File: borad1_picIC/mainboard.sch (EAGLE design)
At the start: 23 parts, among them IC2 7805TV, K1 G6RW

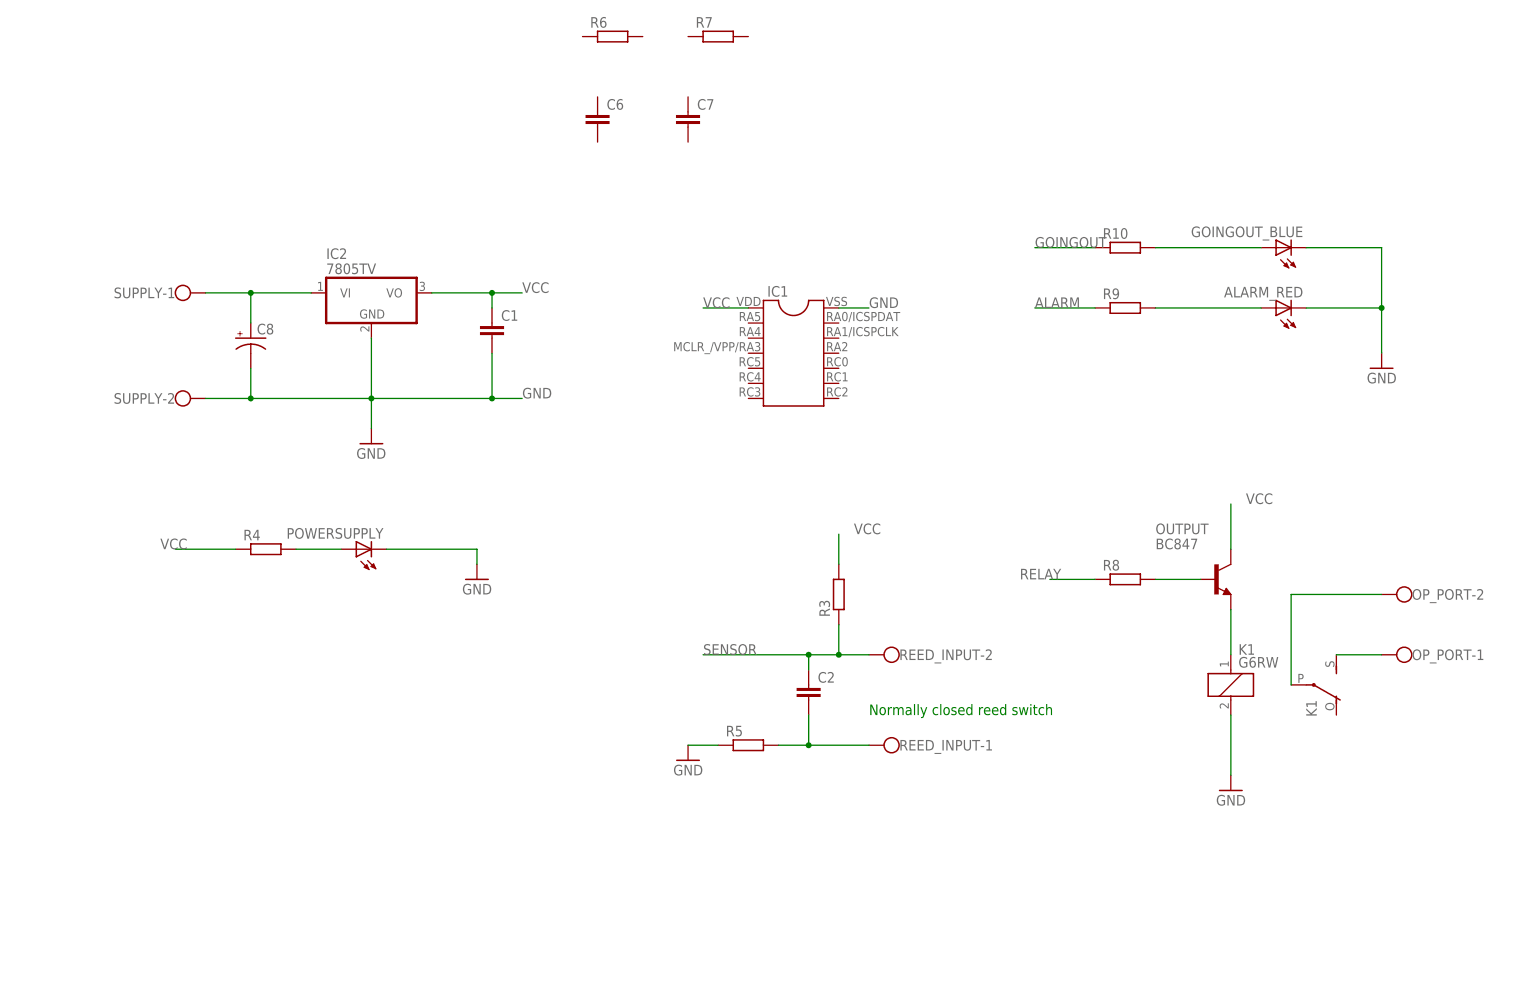
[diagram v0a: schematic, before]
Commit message: First board ready, just figuring out the placement and connectors.
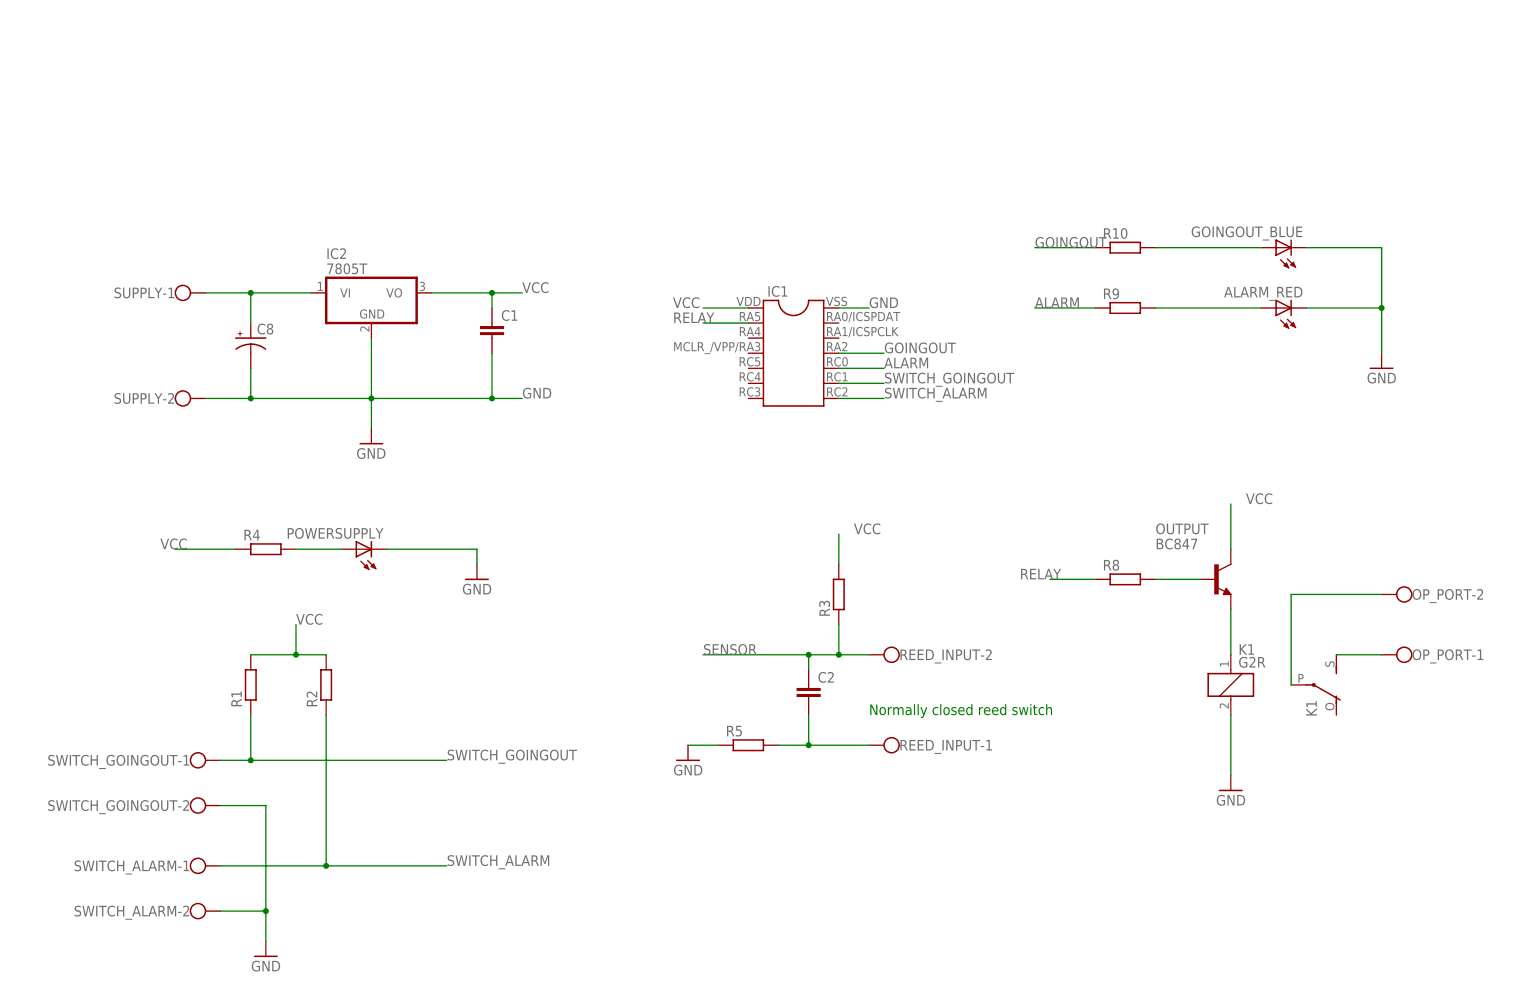
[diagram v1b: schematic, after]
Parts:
- removed C6, C7: (no value), eagle-ltspice:CC0603
- removed R6, R7: (no value), rcl:R-EU_R0603
- added R1, R2: (no value), rcl:R-EU_R0603
- added SWITCH_ALARM, SWITCH_GOINGOUT: (no value), con-wago-500:W237-102
- IC2: value 7805TV -> 7805T; device linear:7805TV -> linear:7805T
- K1: value G6RW -> G2R; device relay:G6RW -> relay:G2R
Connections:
- new net SWITCH_ALARM: IC1.8, R2.1, SWITCH_ALARM-1.KL
- new net SWITCH_GOINGOUT: IC1.9, R1.1, SWITCH_GOINGOUT-1.KL
- net ALARM: now also IC1.10
- net GND: now also SWITCH_ALARM-2.KL, SWITCH_GOINGOUT-2.KL
- net GOINGOUT: now also IC1.11
- net RELAY: now also IC1.2
- net VCC: now also R1.2, R2.2

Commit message: Converting everything thing to SMD, All the wires routed, components and connection modified as per suggestion from senior
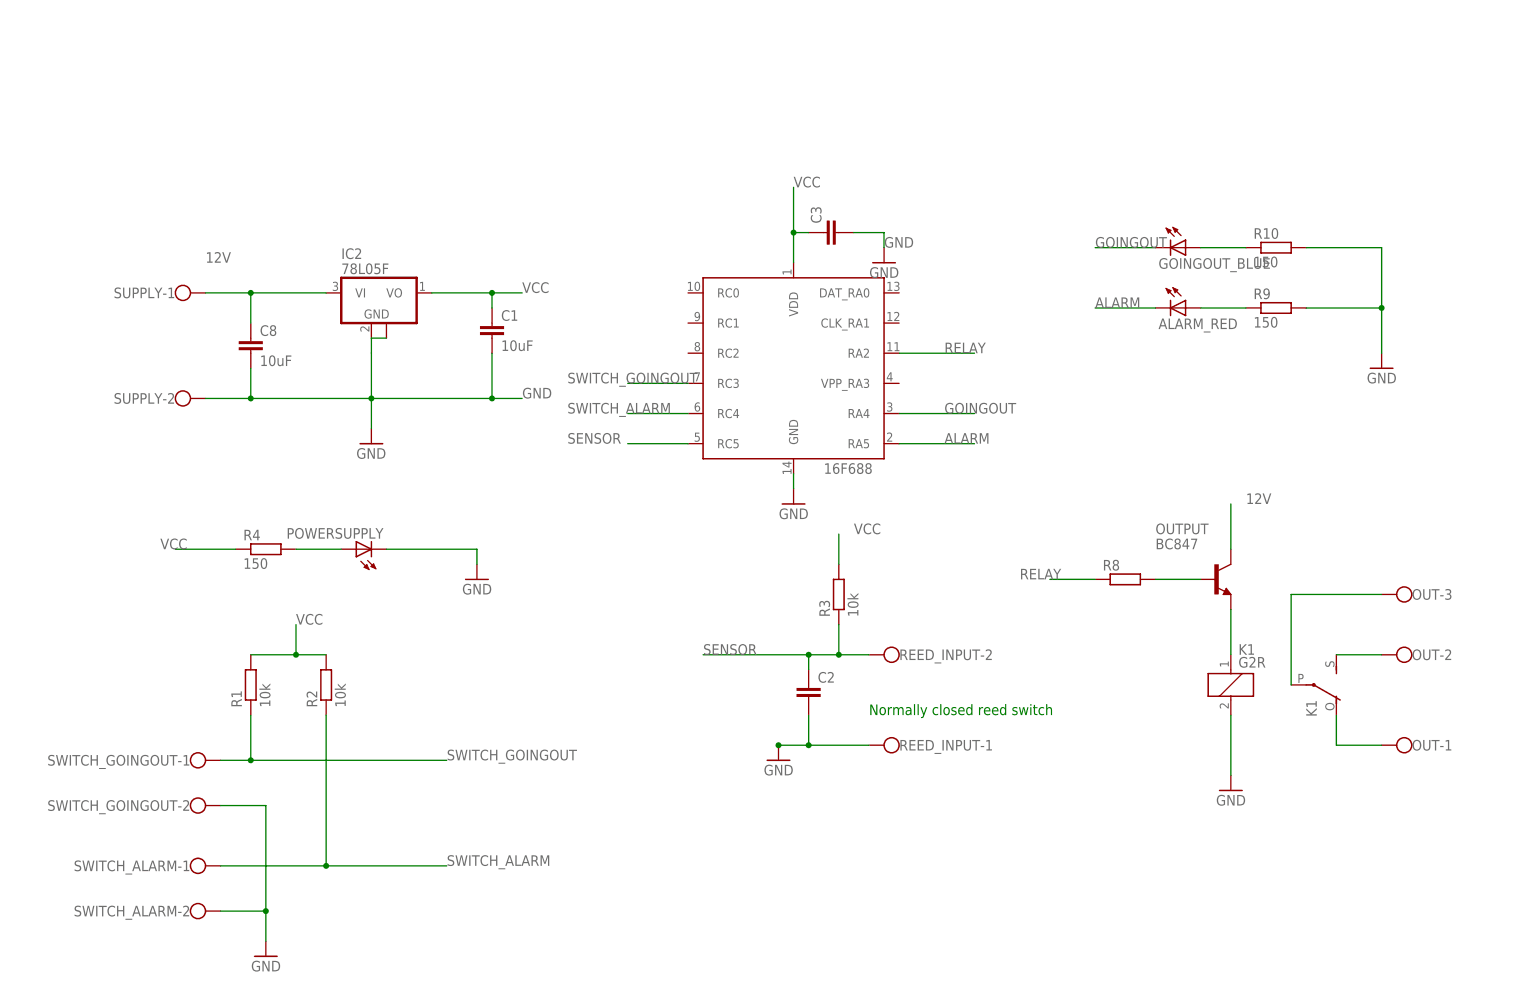
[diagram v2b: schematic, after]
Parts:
- removed IC1: (no value), pic16f1824_mack:DIL14
- removed OP_PORT: (no value), con-wago-500:W237-102
- removed R5: (no value), rcl:R-EU_R0603
- added C3: (no value), rcl:C-EUC0805
- added OUT: (no value), con-wago-500:W237-103
- added U$1: (no value), microchip-16f688:PIC16F688SOIC14
- C1: value (none) -> 10uF; device eagle-ltspice:CC0603 -> rcl:C-EUC0805
- C8: value (none) -> 10uF; device rcl:CPOL-USE2.5-5 -> rcl:C-EUC0805
- IC2: value 7805T -> 78L05F; device linear:7805T -> linear:78L05F
- R1, R2, R3: value (none) -> 10k
- R10, R4, R9: value (none) -> 150
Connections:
- removed net N$7: C2.2, R5.2, REED_INPUT-1.KL
- new net 12V: C8.1, IC2.VI, OUTPUT.C, SUPPLY-1.KL
- net ALARM: now also ALARM_RED.C, U$1.RA5; no longer IC1.10, R9.1
- net GND: now also C2.2, C3.2, C8.2, IC2.GND@1, R10.2, R9.2, REED_INPUT-1.KL, U$1.GND; no longer ALARM_RED.C, C8.-, GOINGOUT_BLUE.C, IC1.14, R5.1
- net GOINGOUT: now also GOINGOUT_BLUE.C, U$1.RA4; no longer IC1.11, R10.1
- net N$1: now also K12.O, OUT-1.KL; no longer C8.+, IC2.VI, SUPPLY-1.KL
- net N$2: now also R10.1; no longer R10.2
- net N$5: now also R9.1; no longer R9.2
- net N$8: now also OUT-3.KL; no longer OP_PORT-2.KL
- net N$9: now also OUT-2.KL; no longer OP_PORT-1.KL
- net RELAY: now also U$1.RA2; no longer IC1.2
- net SENSOR: now also U$1.RC5
- net SWITCH_ALARM: now also U$1.RC4; no longer IC1.8
- net SWITCH_GOINGOUT: now also U$1.RC3; no longer IC1.9
- net VCC: now also C3.1, U$1.VDD; no longer IC1.1, OUTPUT.C
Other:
- moved on the sheet: ALARM_RED, GOINGOUT_BLUE, R10, R9

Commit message: Changing Relay foot print to available relay and rerouted the whole PCB
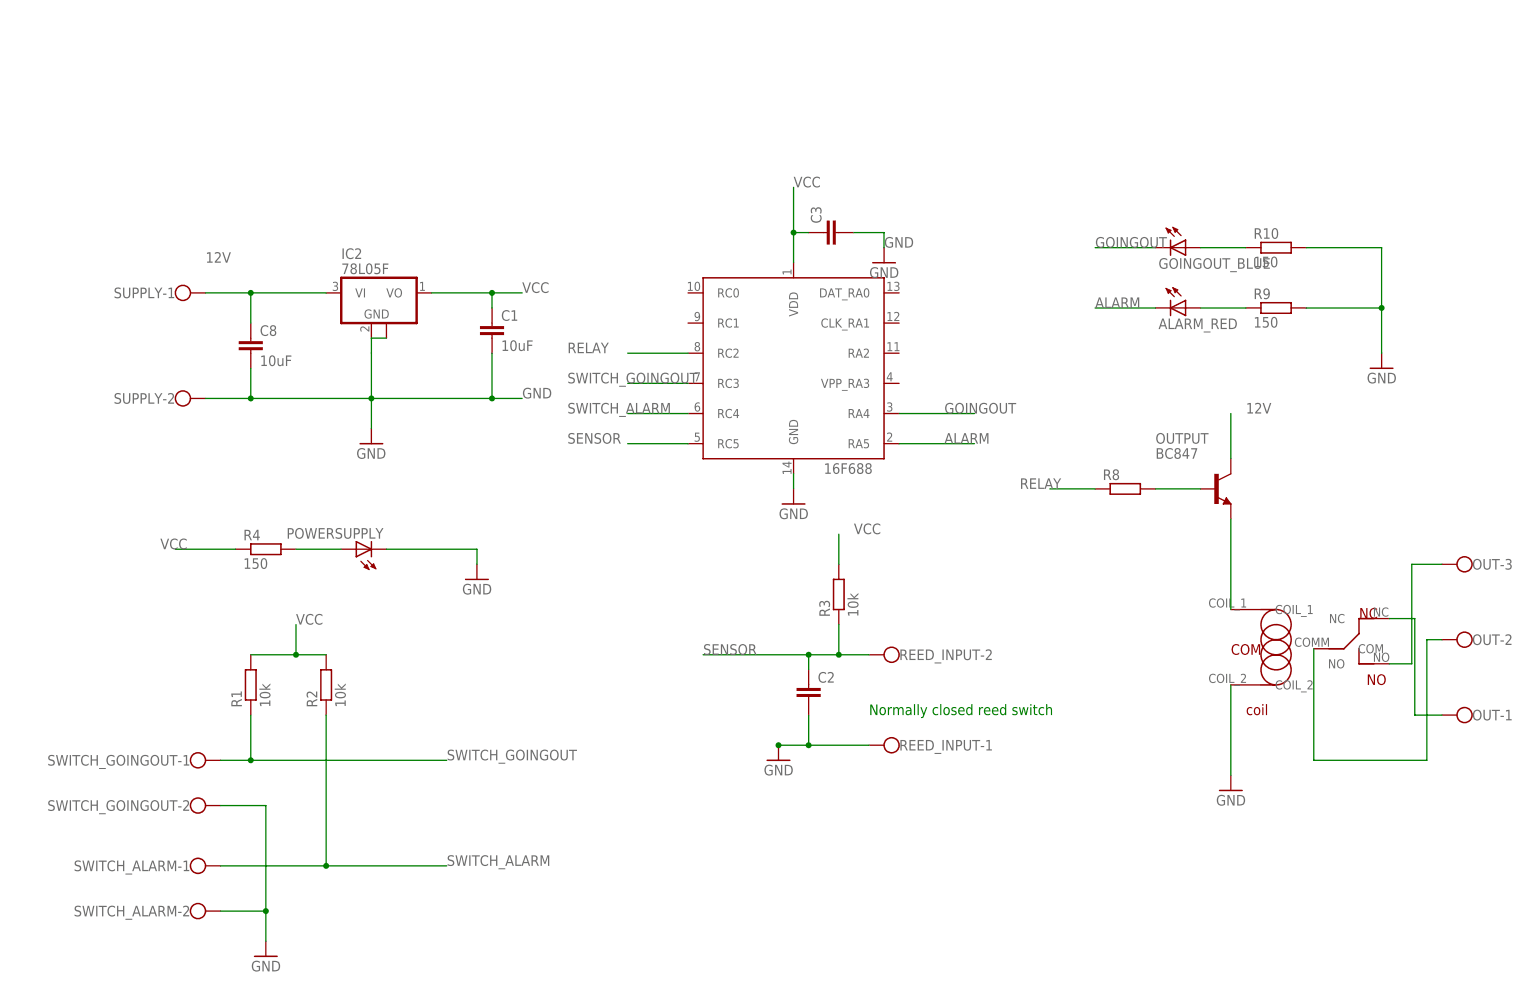
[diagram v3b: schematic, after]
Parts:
- removed K1: G2R, relay:G2R
- added U$2: (no value), JQC-3FC_relay:JQC-3FC_RELAY
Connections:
- net GND: now also U$2.COIL_2; no longer K11.2
- net N$1: now also OUTPUT.E, U$2.COIL_1; no longer K12.O, OUT-1.KL
- net N$6: now also OUT-1.KL, U$2.NC; no longer K11.1, OUTPUT.E
- net N$8: now also U$2.NO; no longer K12.P
- net N$9: now also U$2.COM; no longer K12.S
- net RELAY: now also U$1.RC2; no longer U$1.RA2
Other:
- moved on the sheet: OUT-1, OUT-2, OUT-3, OUTPUT, R8
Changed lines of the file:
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@@
 <?xml version="1.0" encoding="utf-8"?>
 <!DOCTYPE eagle SYSTEM "eagle.dtd">
-<eagle version="7.2.0">
+<eagle version="7.5.0">
 <drawing>
 <settings>
@@
 <part name="ALARM_RED" library="led" deviceset="LED" device="5MM"/>
 <part name="OUTPUT" library="transistor" deviceset="BC847" device=""/>
-<part name="K1" library="relay" deviceset="G2R" device=""/>
 <part name="REED_INPUT" library="con-wago-500" deviceset="W237-102" device=""/>
 <part name="SUPPLY" library="con-wago-500" deviceset="W237-102" device=""/>
@@
 <part name="GND7" library="supply1" deviceset="GND" device=""/>
 <part name="GND8" library="supply1" deviceset="GND" device=""/>
+<part name="U$2" library="JQC-3FC_relay" deviceset="JQC-3FC_RELAY" device=""/>
 </parts>
 <sheets>
@@
 <instance part="R3" gate="G$1" x="134.62" y="71.12" rot="R90"/>
 <instance part="R4" gate="G$1" x="38.1" y="78.74"/>
-<instance part="R8" gate="G$1" x="182.88" y="73.66"/>
+<instance part="R8" gate="G$1" x="182.88" y="88.9"/>
 <instance part="R9" gate="G$1" x="208.28" y="119.38"/>
 <instance part="R10" gate="G$1" x="208.28" y="129.54"/>
@@
 <instance part="GOINGOUT_BLUE" gate="G$1" x="193.04" y="129.54" rot="R270"/>
 <instance part="ALARM_RED" gate="G$1" x="193.04" y="119.38" rot="R270"/>
-<instance part="OUTPUT" gate="G$1" x="198.12" y="73.66"/>
-<instance part="K1" gate="1" x="200.66" y="55.88"/>
-<instance part="K1" gate="2" x="213.36" y="55.88" rot="R270"/>
+<instance part="OUTPUT" gate="G$1" x="198.12" y="88.9"/>
 <instance part="REED_INPUT" gate="-1" x="144.78" y="45.72" rot="R180"/>
 <instance part="REED_INPUT" gate="-2" x="144.78" y="60.96" rot="R180"/>
@@
 <instance part="R2" gate="G$1" x="48.26" y="55.88" rot="R90"/>
 <instance part="GND6" gate="1" x="38.1" y="10.16" rot="MR0"/>
-<instance part="OUT" gate="-1" x="231.14" y="45.72" rot="R180"/>
-<instance part="OUT" gate="-2" x="231.14" y="60.96" rot="R180"/>
-<instance part="OUT" gate="-3" x="231.14" y="71.12" rot="R180"/>
+<instance part="OUT" gate="-1" x="241.3" y="50.8" rot="R180"/>
+<instance part="OUT" gate="-2" x="241.3" y="63.5" rot="R180"/>
+<instance part="OUT" gate="-3" x="241.3" y="76.2" rot="R180"/>
 <instance part="C3" gate="G$1" x="132.08" y="132.08" rot="R90"/>
 <instance part="U$1" gate="NAME" x="127" y="111.76"/>
 <instance part="GND7" gate="1" x="142.24" y="127" rot="MR0"/>
 <instance part="GND8" gate="1" x="127" y="86.36" rot="MR0"/>
+<instance part="U$2" gate="G$1" x="246.38" y="50.8"/>
 </instances>
 <busses>
@@
 <segment>
 <pinref part="OUTPUT" gate="G$1" pin="C"/>
-<wire x1="200.66" y1="78.74" x2="200.66" y2="86.36" width="0.1524" layer="91"/>
-<label x="203.2" y="86.36" size="1.778" layer="95"/>
+<wire x1="200.66" y1="93.98" x2="200.66" y2="101.6" width="0.1524" layer="91"/>
+<label x="203.2" y="101.6" size="1.778" layer="95"/>
 </segment>
 </net>
@@
 </segment>
 <segment>
-<pinref part="K1" gate="1" pin="2"/>
-<wire x1="200.66" y1="50.8" x2="200.66" y2="40.64" width="0.1524" layer="91"/>
-<pinref part="GND3" gate="1" pin="GND"/>
-</segment>
-<segment>
 <wire x1="226.06" y1="129.54" x2="226.06" y2="119.38" width="0.1524" layer="91"/>
 <pinref part="GND4" gate="1" pin="GND"/>
@@
 <wire x1="127" y1="91.44" x2="127" y2="88.9" width="0.1524" layer="91"/>
 </segment>
+<segment>
+<pinref part="GND3" gate="1" pin="GND"/>
+<pinref part="U$2" gate="G$1" pin="COIL_2"/>
+<wire x1="200.66" y1="40.64" x2="200.66" y2="55.88" width="0.1524" layer="91"/>
+</segment>
 </net>
 <net name="N$4" class="0">
@@
 <pinref part="R8" gate="G$1" pin="2"/>
 <pinref part="OUTPUT" gate="G$1" pin="B"/>
-<wire x1="187.96" y1="73.66" x2="195.58" y2="73.66" width="0.1524" layer="91"/>
+<wire x1="187.96" y1="88.9" x2="195.58" y2="88.9" width="0.1524" layer="91"/>
 </segment>
 </net>
@@
 <segment>
 <pinref part="R8" gate="G$1" pin="1"/>
-<wire x1="177.8" y1="73.66" x2="170.18" y2="73.66" width="0.1524" layer="91"/>
-<label x="165.1" y="73.66" size="1.778" layer="95"/>
-</segment>
-<segment>
-<pinref part="U$1" gate="NAME" pin="RA2"/>
-<wire x1="144.78" y1="111.76" x2="157.48" y2="111.76" width="0.1524" layer="91"/>
-<label x="152.4" y="111.76" size="1.778" layer="95"/>
-</segment>
-</net>
-<net name="N$6" class="0">
-<segment>
-<pinref part="OUTPUT" gate="G$1" pin="E"/>
-<pinref part="K1" gate="1" pin="1"/>
-<wire x1="200.66" y1="68.58" x2="200.66" y2="60.96" width="0.1524" layer="91"/>
-</segment>
-</net>
-<net name="N$8" class="0">
-<segment>
-<pinref part="K1" gate="2" pin="P"/>
-<wire x1="210.82" y1="55.88" x2="210.82" y2="71.12" width="0.1524" layer="91"/>
-<wire x1="210.82" y1="71.12" x2="226.06" y2="71.12" width="0.1524" layer="91"/>
-<pinref part="OUT" gate="-3" pin="KL"/>
-</segment>
-</net>
-<net name="N$9" class="0">
-<segment>
-<pinref part="K1" gate="2" pin="S"/>
-<wire x1="218.44" y1="60.96" x2="226.06" y2="60.96" width="0.1524" layer="91"/>
-<pinref part="OUT" gate="-2" pin="KL"/>
+<wire x1="177.8" y1="88.9" x2="170.18" y2="88.9" width="0.1524" layer="91"/>
+<label x="165.1" y="88.9" size="1.778" layer="95"/>
+</segment>
+<segment>
+<pinref part="U$1" gate="NAME" pin="RC2"/>
+<wire x1="109.22" y1="111.76" x2="99.06" y2="111.76" width="0.1524" layer="91"/>
+<label x="88.9" y="111.76" size="1.778" layer="95"/>
 </segment>
 </net>
@@
 </segment>
 </net>
-<net name="N$1" class="0">
-<segment>
-<pinref part="K1" gate="2" pin="O"/>
-<pinref part="OUT" gate="-1" pin="KL"/>
-<wire x1="218.44" y1="50.8" x2="218.44" y2="45.72" width="0.1524" layer="91"/>
-<wire x1="218.44" y1="45.72" x2="226.06" y2="45.72" width="0.1524" layer="91"/>
-</segment>
-</net>
 <net name="N$2" class="0">
 <segment>
@@
 </segment>
 </net>
+<net name="N$1" class="0">
+<segment>
+<pinref part="U$2" gate="G$1" pin="COIL_1"/>
+<pinref part="OUTPUT" gate="G$1" pin="E"/>
+<wire x1="200.66" y1="68.58" x2="200.66" y2="83.82" width="0.1524" layer="91"/>
+</segment>
+</net>
+<net name="N$9" class="0">
+<segment>
+<pinref part="OUT" gate="-2" pin="KL"/>
+<wire x1="236.22" y1="63.5" x2="233.68" y2="63.5" width="0.1524" layer="91"/>
+<wire x1="233.68" y1="63.5" x2="233.68" y2="43.18" width="0.1524" layer="91"/>
+<wire x1="233.68" y1="43.18" x2="214.63" y2="43.18" width="0.1524" layer="91"/>
+<pinref part="U$2" gate="G$1" pin="COM"/>
+<wire x1="214.63" y1="43.18" x2="214.63" y2="61.976" width="0.1524" layer="91"/>
+</segment>
+</net>
+<net name="N$6" class="0">
+<segment>
+<pinref part="OUT" gate="-1" pin="KL"/>
+<wire x1="236.22" y1="50.8" x2="231.648" y2="50.8" width="0.1524" layer="91"/>
+<wire x1="231.648" y1="50.8" x2="231.648" y2="67.056" width="0.1524" layer="91"/>
+<pinref part="U$2" gate="G$1" pin="NC"/>
+<wire x1="231.648" y1="67.056" x2="227.33" y2="67.056" width="0.1524" layer="91"/>
+</segment>
+</net>
+<net name="N$8" class="0">
+<segment>
+<pinref part="U$2" gate="G$1" pin="NO"/>
+<wire x1="227.33" y1="59.436" x2="231.14" y2="59.436" width="0.1524" layer="91"/>
+<wire x1="231.14" y1="59.436" x2="231.14" y2="76.2" width="0.1524" layer="91"/>
+<pinref part="OUT" gate="-3" pin="KL"/>
+<wire x1="231.14" y1="76.2" x2="236.22" y2="76.2" width="0.1524" layer="91"/>
+</segment>
+</net>
